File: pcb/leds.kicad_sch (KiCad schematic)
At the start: 0 parts

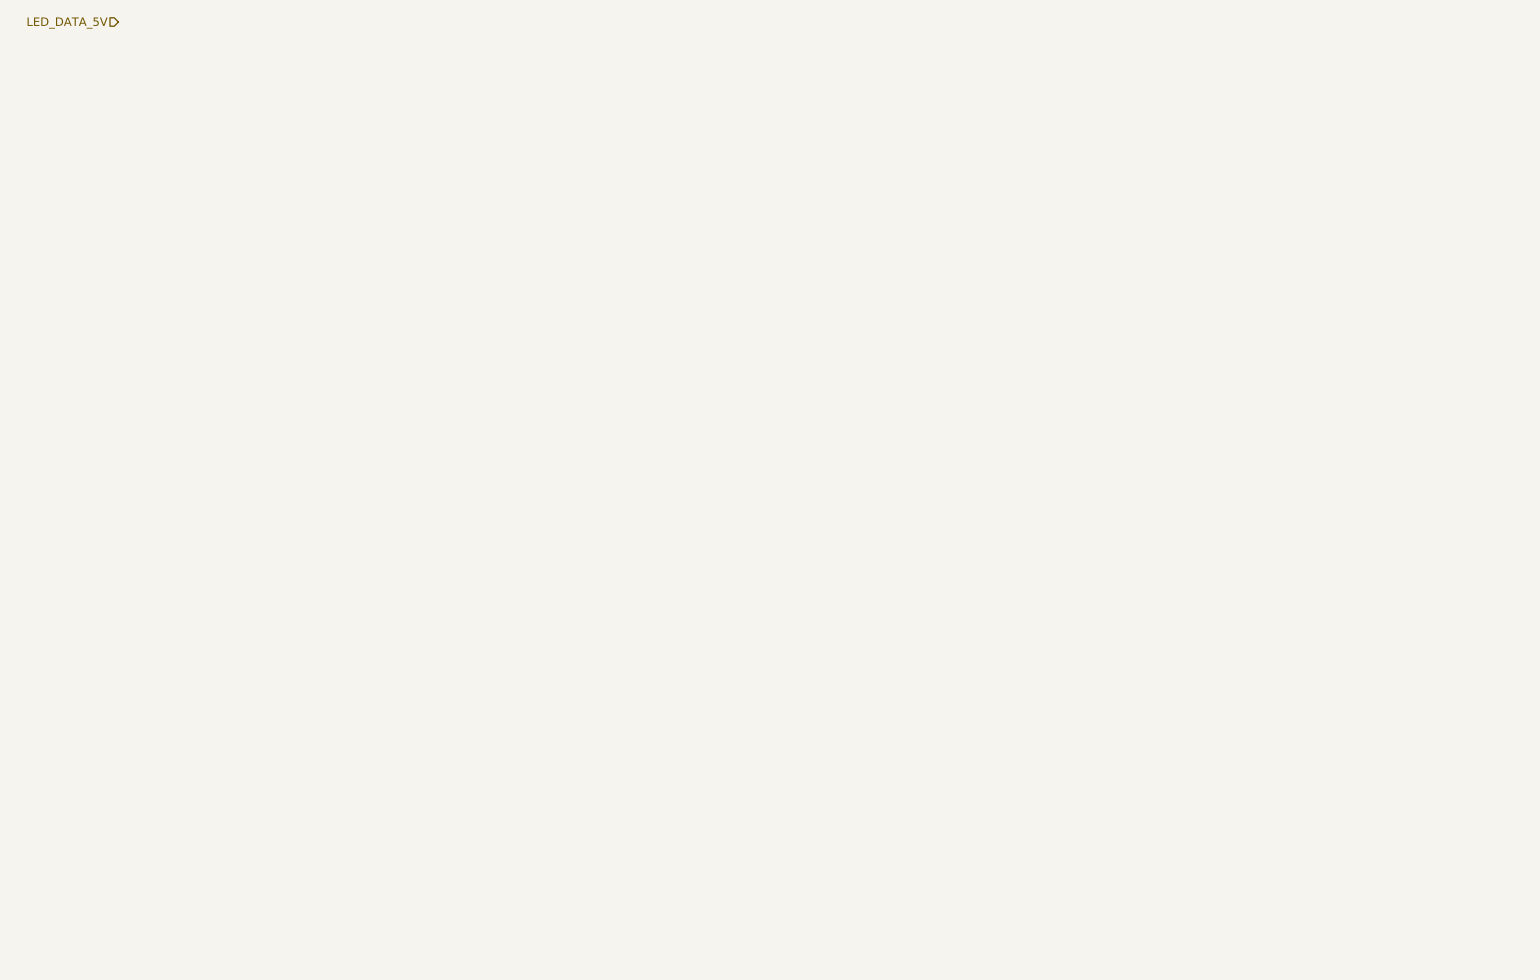
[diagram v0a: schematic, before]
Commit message: Started adding leds and started making pcbs.
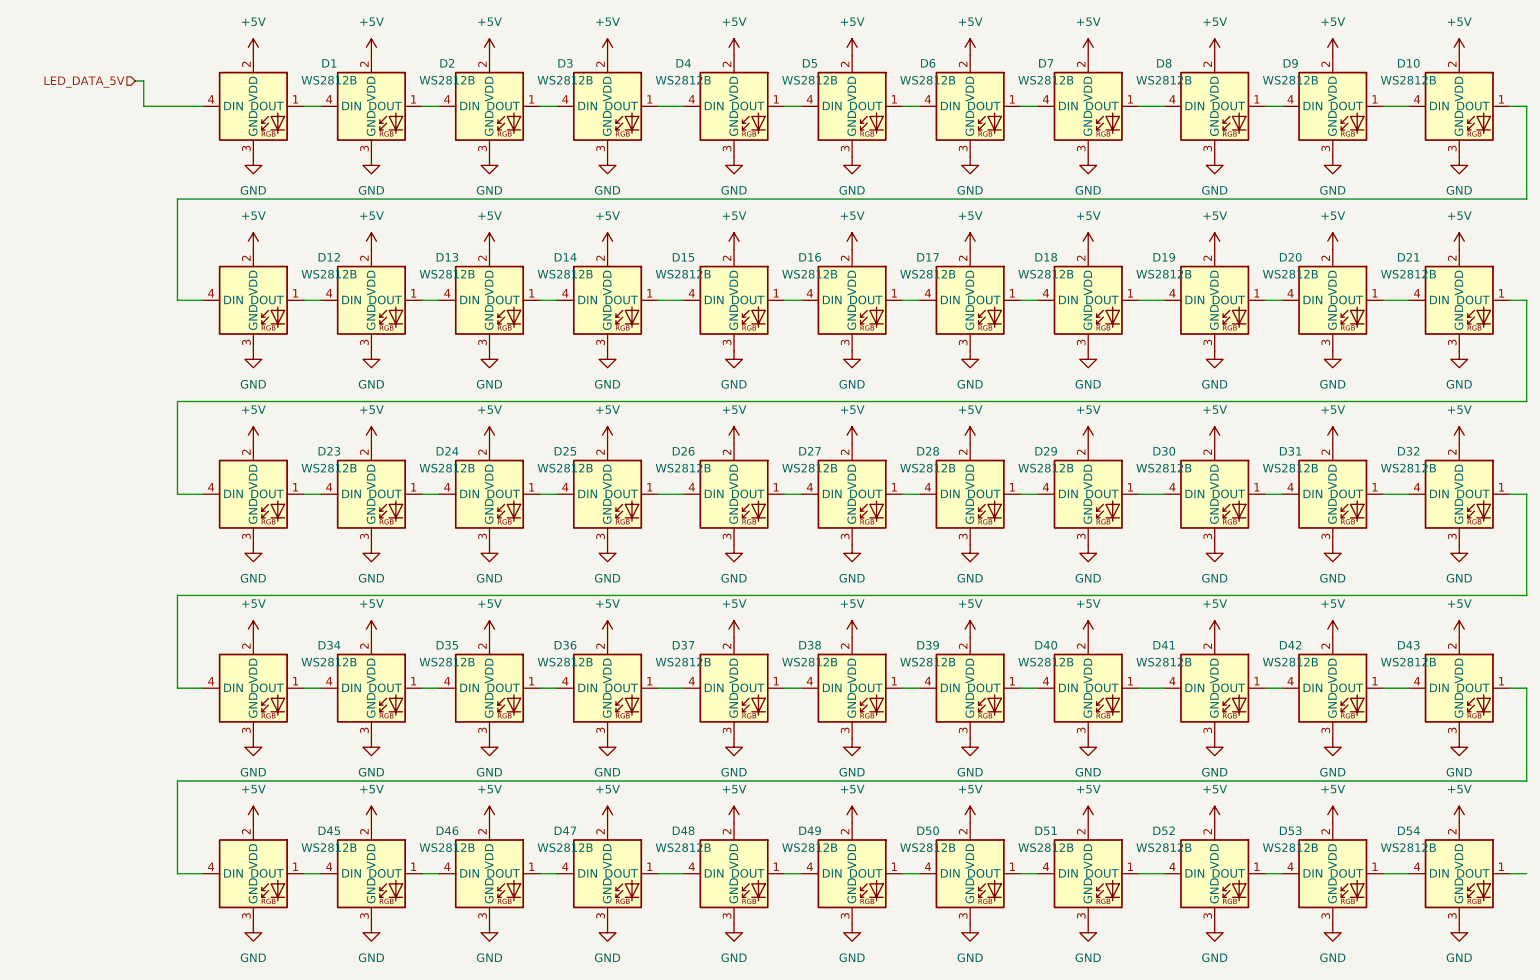
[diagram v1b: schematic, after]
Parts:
- added D1, D10, D11, D12, D13, D14, D15, D16, D17, D18, D19, D2, D20, D21, D22, D23, D24, D25, D26, D27, D28, D29, D3, D30, D31, D32, D33, D34, D35, D36, D37, D38, D39, D4, D40, D41, D42, D43, D44, D45, D46, D47, D48, D49, D5, D50, D51, D52, D53, D54, D55, D6, D7, D8, D9: WS2812B, PCM_JLCPCB:LED-SMD_4P-L1.6-W1.5_XL-1615RGBC-WS2812B, symbol PCM_JLCPCB-Extended:LED, WS2812B, 1615
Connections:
- net LED_DATA_5V: now also D1.4 (DIN)
- new net: D37.1 (DOUT), D38.4 (DIN)
- new net: D36.1 (DOUT), D37.4 (DIN)
- new net: D23.1 (DOUT), D24.4 (DIN)
- new net: D22.1 (DOUT), D23.4 (DIN)
- new net: D10.4 (DIN), D9.1 (DOUT)
- new net: D8.1 (DOUT), D9.4 (DIN)
- new net: D25.1 (DOUT), D26.4 (DIN)
- new net: D24.1 (DOUT), D25.4 (DIN)
- new net: D27.1 (DOUT), D28.4 (DIN)
- new net: D26.1 (DOUT), D27.4 (DIN)
- new net: D1.1 (DOUT), D2.4 (DIN)
- new net: D41.1 (DOUT), D42.4 (DIN)
- new net: D40.1 (DOUT), D41.4 (DIN)
- new net: D5.1 (DOUT), D6.4 (DIN)
- new net: D4.1 (DOUT), D5.4 (DIN)
- new net: D3.1 (DOUT), D4.4 (DIN)
- new net: D46.1 (DOUT), D47.4 (DIN)
- new net: D45.1 (DOUT), D46.4 (DIN)
- new net: D6.1 (DOUT), D7.4 (DIN)
- new net: D43.1 (DOUT), D44.4 (DIN)
- new net: D42.1 (DOUT), D43.4 (DIN)
- new net: D7.1 (DOUT), D8.4 (DIN)
- new net: D13.1 (DOUT), D14.4 (DIN)
- new net: D12.1 (DOUT), D13.4 (DIN)
- new net: D14.1 (DOUT), D15.4 (DIN)
- new net: D17.1 (DOUT), D18.4 (DIN)
- new net: D16.1 (DOUT), D17.4 (DIN)
- new net: D54.1 (DOUT), D55.4 (DIN)
- new net: D53.1 (DOUT), D54.4 (DIN)
- new net: D10.1 (DOUT), D11.4 (DIN)
- new net: D18.1 (DOUT), D19.4 (DIN)
- new net: D20.1 (DOUT), D21.4 (DIN)
- new net: D19.1 (DOUT), D20.4 (DIN)
- new net: D34.1 (DOUT), D35.4 (DIN)
- new net: D33.1 (DOUT), D34.4 (DIN)
- new net: D49.1 (DOUT), D50.4 (DIN)
- new net: D48.1 (DOUT), D49.4 (DIN)
- new net: D11.1 (DOUT), D12.4 (DIN)
- new net: D47.1 (DOUT), D48.4 (DIN)
- new net: D44.1 (DOUT), D45.4 (DIN)
- new net: D39.1 (DOUT), D40.4 (DIN)
- new net: D38.1 (DOUT), D39.4 (DIN)
- new net: D30.1 (DOUT), D31.4 (DIN)
- new net: D29.1 (DOUT), D30.4 (DIN)
- new net: D2.1 (DOUT), D3.4 (DIN)
- new net: D50.1 (DOUT), D51.4 (DIN)
- new net: D52.1 (DOUT), D53.4 (DIN)
- new net: D15.1 (DOUT), D16.4 (DIN)
- new net: D51.1 (DOUT), D52.4 (DIN)
- new net: D31.1 (DOUT), D32.4 (DIN)
- new net: D21.1 (DOUT), D22.4 (DIN)
- new net: D32.1 (DOUT), D33.4 (DIN)
- new net: D35.1 (DOUT), D36.4 (DIN)
- new net: D28.1 (DOUT), D29.4 (DIN)
- new net +5V: D1.2 (VDD), D10.2 (VDD), D11.2 (VDD), D12.2 (VDD), D13.2 (VDD), D14.2 (VDD), D15.2 (VDD), D16.2 (VDD), D17.2 (VDD), D18.2 (VDD), D19.2 (VDD), D2.2 (VDD), D20.2 (VDD), D21.2 (VDD), D22.2 (VDD), D23.2 (VDD), D24.2 (VDD), D25.2 (VDD), D26.2 (VDD), D27.2 (VDD), D28.2 (VDD), D29.2 (VDD), D3.2 (VDD), D30.2 (VDD), D31.2 (VDD), D32.2 (VDD), D33.2 (VDD), D34.2 (VDD), D35.2 (VDD), D36.2 (VDD), D37.2 (VDD), D38.2 (VDD), D39.2 (VDD), D4.2 (VDD), D40.2 (VDD), D41.2 (VDD), D42.2 (VDD), D43.2 (VDD), D44.2 (VDD), D45.2 (VDD), D46.2 (VDD), D47.2 (VDD), D48.2 (VDD), D49.2 (VDD), D5.2 (VDD), D50.2 (VDD), D51.2 (VDD), D52.2 (VDD), D53.2 (VDD), D54.2 (VDD), D55.2 (VDD), D6.2 (VDD), D7.2 (VDD), D8.2 (VDD), D9.2 (VDD)
- new net GND: D1.3 (GND), D10.3 (GND), D11.3 (GND), D12.3 (GND), D13.3 (GND), D14.3 (GND), D15.3 (GND), D16.3 (GND), D17.3 (GND), D18.3 (GND), D19.3 (GND), D2.3 (GND), D20.3 (GND), D21.3 (GND), D22.3 (GND), D23.3 (GND), D24.3 (GND), D25.3 (GND), D26.3 (GND), D27.3 (GND), D28.3 (GND), D29.3 (GND), D3.3 (GND), D30.3 (GND), D31.3 (GND), D32.3 (GND), D33.3 (GND), D34.3 (GND), D35.3 (GND), D36.3 (GND), D37.3 (GND), D38.3 (GND), D39.3 (GND), D4.3 (GND), D40.3 (GND), D41.3 (GND), D42.3 (GND), D43.3 (GND), D44.3 (GND), D45.3 (GND), D46.3 (GND), D47.3 (GND), D48.3 (GND), D49.3 (GND), D5.3 (GND), D50.3 (GND), D51.3 (GND), D52.3 (GND), D53.3 (GND), D54.3 (GND), D55.3 (GND), D6.3 (GND), D7.3 (GND), D8.3 (GND), D9.3 (GND)

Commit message: server updates and battling with kicad
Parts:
- removed D10, D11, D12, D13, D14, D15, D16, D17, D18, D19, D2, D20, D21, D22, D23, D24, D25, D26, D27, D28, D29, D3, D30, D31, D32, D33, D34, D35, D36, D37, D38, D39, D4, D40, D41, D42, D43, D44, D45, D46, D47, D48, D49, D5, D50, D51, D52, D53, D54, D55, D6, D7, D8, D9: WS2812B, PCM_JLCPCB:LED-SMD_4P-L1.6-W1.5_XL-1615RGBC-WS2812B, symbol PCM_JLCPCB-Extended:LED, WS2812B, 1615
- added D102, D103, D104, D105, D106, D107, D108, D109, D110, D111, D112, D113, D114, D115, D116, D117, D118, D119, D120, D121, D122, D123, D124, D125, D126, D127, D128, D129, D130, D131, D132, D133, D134, D135, D136, D137, D138, D139, D140, D141, D142, D143, D144, D145, D146, D147, D148, D149, D150, D151, D152, D153, D154, D155, D156, D157, D158, D159, D160, D161, D162, D163, D164, D165, D166, D167, D168, D169, D170, D171, D172, D173, D174, D175, D176, D177, D178, D179, D180, D181, D182, D183, D184, D185, D186, D187, D188, D189, D190, D191, D192, D193, D194, D195, D196, D197, D198, D199, D200: WS2812B, PCM_JLCPCB:LED-SMD_4P-L1.6-W1.5_XL-1615RGBC-WS2812B, symbol PCM_JLCPCB-Extended:LED, WS2812B, 1615
- renumbered D1 to D101
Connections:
- net +5V: now also D102.2 (VDD), D103.2 (VDD), D104.2 (VDD), D105.2 (VDD), D106.2 (VDD), D107.2 (VDD), D108.2 (VDD), D109.2 (VDD), D110.2 (VDD), D111.2 (VDD), D112.2 (VDD), D113.2 (VDD), D114.2 (VDD), D115.2 (VDD), D116.2 (VDD), D117.2 (VDD), D118.2 (VDD), D119.2 (VDD), D120.2 (VDD), D121.2 (VDD), D122.2 (VDD), D123.2 (VDD), D124.2 (VDD), D125.2 (VDD), D126.2 (VDD), D127.2 (VDD), D128.2 (VDD), D129.2 (VDD), D130.2 (VDD), D131.2 (VDD), D132.2 (VDD), D133.2 (VDD), D134.2 (VDD), D135.2 (VDD), D136.2 (VDD), D137.2 (VDD), D138.2 (VDD), D139.2 (VDD), D140.2 (VDD), D141.2 (VDD), D142.2 (VDD), D143.2 (VDD), D144.2 (VDD), D145.2 (VDD), D146.2 (VDD), D147.2 (VDD), D148.2 (VDD), D149.2 (VDD), D150.2 (VDD), D151.2 (VDD), D152.2 (VDD), D153.2 (VDD), D154.2 (VDD), D155.2 (VDD), D156.2 (VDD), D157.2 (VDD), D158.2 (VDD), D159.2 (VDD), D160.2 (VDD), D161.2 (VDD), D162.2 (VDD), D163.2 (VDD), D164.2 (VDD), D165.2 (VDD), D166.2 (VDD), D167.2 (VDD), D168.2 (VDD), D169.2 (VDD), D170.2 (VDD), D171.2 (VDD), D172.2 (VDD), D173.2 (VDD), D174.2 (VDD), D175.2 (VDD), D176.2 (VDD), D177.2 (VDD), D178.2 (VDD), D179.2 (VDD), D180.2 (VDD), D181.2 (VDD), D182.2 (VDD), D183.2 (VDD), D184.2 (VDD), D185.2 (VDD), D186.2 (VDD), D187.2 (VDD), D188.2 (VDD), D189.2 (VDD), D190.2 (VDD), D191.2 (VDD), D192.2 (VDD), D193.2 (VDD), D194.2 (VDD), D195.2 (VDD), D196.2 (VDD), D197.2 (VDD), D198.2 (VDD), D199.2 (VDD), D200.2 (VDD)
- net GND: now also D102.3 (GND), D103.3 (GND), D104.3 (GND), D105.3 (GND), D106.3 (GND), D107.3 (GND), D108.3 (GND), D109.3 (GND), D110.3 (GND), D111.3 (GND), D112.3 (GND), D113.3 (GND), D114.3 (GND), D115.3 (GND), D116.3 (GND), D117.3 (GND), D118.3 (GND), D119.3 (GND), D120.3 (GND), D121.3 (GND), D122.3 (GND), D123.3 (GND), D124.3 (GND), D125.3 (GND), D126.3 (GND), D127.3 (GND), D128.3 (GND), D129.3 (GND), D130.3 (GND), D131.3 (GND), D132.3 (GND), D133.3 (GND), D134.3 (GND), D135.3 (GND), D136.3 (GND), D137.3 (GND), D138.3 (GND), D139.3 (GND), D140.3 (GND), D141.3 (GND), D142.3 (GND), D143.3 (GND), D144.3 (GND), D145.3 (GND), D146.3 (GND), D147.3 (GND), D148.3 (GND), D149.3 (GND), D150.3 (GND), D151.3 (GND), D152.3 (GND), D153.3 (GND), D154.3 (GND), D155.3 (GND), D156.3 (GND), D157.3 (GND), D158.3 (GND), D159.3 (GND), D160.3 (GND), D161.3 (GND), D162.3 (GND), D163.3 (GND), D164.3 (GND), D165.3 (GND), D166.3 (GND), D167.3 (GND), D168.3 (GND), D169.3 (GND), D170.3 (GND), D171.3 (GND), D172.3 (GND), D173.3 (GND), D174.3 (GND), D175.3 (GND), D176.3 (GND), D177.3 (GND), D178.3 (GND), D179.3 (GND), D180.3 (GND), D181.3 (GND), D182.3 (GND), D183.3 (GND), D184.3 (GND), D185.3 (GND), D186.3 (GND), D187.3 (GND), D188.3 (GND), D189.3 (GND), D190.3 (GND), D191.3 (GND), D192.3 (GND), D193.3 (GND), D194.3 (GND), D195.3 (GND), D196.3 (GND), D197.3 (GND), D198.3 (GND), D199.3 (GND), D200.3 (GND)
- net at D101.1 (DOUT): now also D102.4 (DIN)
- new net: D134.1 (DOUT), D135.4 (DIN)
- new net: D133.1 (DOUT), D134.4 (DIN)
- new net: D187.1 (DOUT), D188.4 (DIN)
- new net: D186.1 (DOUT), D187.4 (DIN)
- new net: D160.1 (DOUT), D161.4 (DIN)
- new net: D159.1 (DOUT), D160.4 (DIN)
- new net: D149.1 (DOUT), D150.4 (DIN)
- new net: D148.1 (DOUT), D149.4 (DIN)
- new net: D180.1 (DOUT), D181.4 (DIN)
- new net: D179.1 (DOUT), D180.4 (DIN)
- new net: D116.1 (DOUT), D117.4 (DIN)
- new net: D115.1 (DOUT), D116.4 (DIN)
- new net: D195.1 (DOUT), D196.4 (DIN)
- new net: D194.1 (DOUT), D195.4 (DIN)
- new net: D141.1 (DOUT), D142.4 (DIN)
- new net: D140.1 (DOUT), D141.4 (DIN)
- new net: D163.1 (DOUT), D164.4 (DIN)
- new net: D162.1 (DOUT), D163.4 (DIN)
- new net: D193.1 (DOUT), D194.4 (DIN)
- new net: D192.1 (DOUT), D193.4 (DIN)
- new net: D183.1 (DOUT), D184.4 (DIN)
- new net: D182.1 (DOUT), D183.4 (DIN)
- new net: D161.1 (DOUT), D162.4 (DIN)
- new net: D171.1 (DOUT), D172.4 (DIN)
- new net: D170.1 (DOUT), D171.4 (DIN)
- new net: D185.1 (DOUT), D186.4 (DIN)
- new net: D132.1 (DOUT), D133.4 (DIN)
- new net: D165.1 (DOUT), D166.4 (DIN)
- new net: D164.1 (DOUT), D165.4 (DIN)
- new net: D156.1 (DOUT), D157.4 (DIN)
- new net: D155.1 (DOUT), D156.4 (DIN)
- new net: D181.1 (DOUT), D182.4 (DIN)
- new net: D113.1 (DOUT), D114.4 (DIN)
- new net: D112.1 (DOUT), D113.4 (DIN)
- new net: D138.1 (DOUT), D139.4 (DIN)
- new net: D137.1 (DOUT), D138.4 (DIN)
- new net: D168.1 (DOUT), D169.4 (DIN)
- new net: D167.1 (DOUT), D168.4 (DIN)
- new net: D197.1 (DOUT), D198.4 (DIN)
- new net: D196.1 (DOUT), D197.4 (DIN)
- new net: D188.1 (DOUT), D189.4 (DIN)
- new net: D199.1 (DOUT), D200.4 (DIN)
- new net: D126.1 (DOUT), D127.4 (DIN)
- new net: D125.1 (DOUT), D126.4 (DIN)
- new net: D106.1 (DOUT), D107.4 (DIN)
- new net: D105.1 (DOUT), D106.4 (DIN)
- new net: D108.1 (DOUT), D109.4 (DIN)
- new net: D107.1 (DOUT), D108.4 (DIN)
- new net: D169.1 (DOUT), D170.4 (DIN)
- new net: D109.1 (DOUT), D110.4 (DIN)
- new net: D103.1 (DOUT), D104.4 (DIN)
- new net: D102.1 (DOUT), D103.4 (DIN)
- new net: D198.1 (DOUT), D199.4 (DIN)
- new net: D111.1 (DOUT), D112.4 (DIN)
- new net: D110.1 (DOUT), D111.4 (DIN)
- new net: D118.1 (DOUT), D119.4 (DIN)
- new net: D117.1 (DOUT), D118.4 (DIN)
- new net: D130.1 (DOUT), D131.4 (DIN)
- new net: D129.1 (DOUT), D130.4 (DIN)
- new net: D178.1 (DOUT), D179.4 (DIN)
- new net: D114.1 (DOUT), D115.4 (DIN)
- new net: D158.1 (DOUT), D159.4 (DIN)
- new net: D157.1 (DOUT), D158.4 (DIN)
- new net: D144.1 (DOUT), D145.4 (DIN)
- new net: D143.1 (DOUT), D144.4 (DIN)
- new net: D189.1 (DOUT), D190.4 (DIN)
- new net: D147.1 (DOUT), D148.4 (DIN)
- new net: D146.1 (DOUT), D147.4 (DIN)
- new net: D151.1 (DOUT), D152.4 (DIN)
- new net: D150.1 (DOUT), D151.4 (DIN)
- new net: D190.1 (DOUT), D191.4 (DIN)
- new net: D119.1 (DOUT), D120.4 (DIN)
- new net: D124.1 (DOUT), D125.4 (DIN)
- new net: D122.1 (DOUT), D123.4 (DIN)
- new net: D121.1 (DOUT), D122.4 (DIN)
- new net: D174.1 (DOUT), D175.4 (DIN)
- new net: D173.1 (DOUT), D174.4 (DIN)
- new net: D184.1 (DOUT), D185.4 (DIN)
- new net: D172.1 (DOUT), D173.4 (DIN)
- new net: D142.1 (DOUT), D143.4 (DIN)
- new net: D123.1 (DOUT), D124.4 (DIN)
- new net: D128.1 (DOUT), D129.4 (DIN)
- new net: D175.1 (DOUT), D176.4 (DIN)
- new net: D120.1 (DOUT), D121.4 (DIN)
- new net: D154.1 (DOUT), D155.4 (DIN)
- new net: D153.1 (DOUT), D154.4 (DIN)
- new net: D145.1 (DOUT), D146.4 (DIN)
- new net: D166.1 (DOUT), D167.4 (DIN)
- new net: D135.1 (DOUT), D136.4 (DIN)
- new net: D152.1 (DOUT), D153.4 (DIN)
- new net: D131.1 (DOUT), D132.4 (DIN)
- new net: D104.1 (DOUT), D105.4 (DIN)
- new net: D177.1 (DOUT), D178.4 (DIN)
- new net: D139.1 (DOUT), D140.4 (DIN)
- new net: D191.1 (DOUT), D192.4 (DIN)
- new net: D136.1 (DOUT), D137.4 (DIN)
- new net: D176.1 (DOUT), D177.4 (DIN)
- new net: D127.1 (DOUT), D128.4 (DIN)
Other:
- moved on the sheet: D101

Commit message: finished pcb routing
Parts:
- added D201, D202, D203, D204, D205, D206, D207, D208, D209, D210, D211, D212, D213, D214, D215, D216, D217, D218, D219, D220, D221, D222, D223, D224, D225, D226, D227, D228, D229, D230, D231, D232, D233, D234, D235, D236, D237, D238, D239, D240, D241, D242, D243, D244, D245, D246, D247, D248, D249, D250, D251, D252, D253, D254, D255, D256, D257, D258, D259, D260, D261, D262, D263, D264, D265, D266, D267, D268, D269, D270, D271, D272, D273, D274, D275, D276, D277, D278, D279, D280, D281, D282, D283, D284, D285, D286, D287, D288, D289, D290, D291, D292, D293, D294, D295, D296, D297, D298, D299, D300, D301, D302, D303, D304, D305, D306, D307, D308, D309, D310, D311, D312, D313, D314, D315, D316, D317, D318, D319, D320, D321, D322, D323, D324, D325, D326, D327, D328, D329, D330, D331, D332, D333, D334, D335, D336, D337, D338, D339: WS2812B, PCM_JLCPCB:LED-SMD_4P-L1.6-W1.5_XL-1615RGBC-WS2812B, symbol PCM_JLCPCB-Extended:LED, WS2812B, 1615
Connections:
- net +5V: now also D201.2 (VDD), D202.2 (VDD), D203.2 (VDD), D204.2 (VDD), D205.2 (VDD), D206.2 (VDD), D207.2 (VDD), D208.2 (VDD), D209.2 (VDD), D210.2 (VDD), D211.2 (VDD), D212.2 (VDD), D213.2 (VDD), D214.2 (VDD), D215.2 (VDD), D216.2 (VDD), D217.2 (VDD), D218.2 (VDD), D219.2 (VDD), D220.2 (VDD), D221.2 (VDD), D222.2 (VDD), D223.2 (VDD), D224.2 (VDD), D225.2 (VDD), D226.2 (VDD), D227.2 (VDD), D228.2 (VDD), D229.2 (VDD), D230.2 (VDD), D231.2 (VDD), D232.2 (VDD), D233.2 (VDD), D234.2 (VDD), D235.2 (VDD), D236.2 (VDD), D237.2 (VDD), D238.2 (VDD), D239.2 (VDD), D240.2 (VDD), D241.2 (VDD), D242.2 (VDD), D243.2 (VDD), D244.2 (VDD), D245.2 (VDD), D246.2 (VDD), D247.2 (VDD), D248.2 (VDD), D249.2 (VDD), D250.2 (VDD), D251.2 (VDD), D252.2 (VDD), D253.2 (VDD), D254.2 (VDD), D255.2 (VDD), D256.2 (VDD), D257.2 (VDD), D258.2 (VDD), D259.2 (VDD), D260.2 (VDD), D261.2 (VDD), D262.2 (VDD), D263.2 (VDD), D264.2 (VDD), D265.2 (VDD), D266.2 (VDD), D267.2 (VDD), D268.2 (VDD), D269.2 (VDD), D270.2 (VDD), D271.2 (VDD), D272.2 (VDD), D273.2 (VDD), D274.2 (VDD), D275.2 (VDD), D276.2 (VDD), D277.2 (VDD), D278.2 (VDD), D279.2 (VDD), D280.2 (VDD), D281.2 (VDD), D282.2 (VDD), D283.2 (VDD), D284.2 (VDD), D285.2 (VDD), D286.2 (VDD), D287.2 (VDD), D288.2 (VDD), D289.2 (VDD), D290.2 (VDD), D291.2 (VDD), D292.2 (VDD), D293.2 (VDD), D294.2 (VDD), D295.2 (VDD), D296.2 (VDD), D297.2 (VDD), D298.2 (VDD), D299.2 (VDD), D300.2 (VDD), D301.2 (VDD), D302.2 (VDD), D303.2 (VDD), D304.2 (VDD), D305.2 (VDD), D306.2 (VDD), D307.2 (VDD), D308.2 (VDD), D309.2 (VDD), D310.2 (VDD), D311.2 (VDD), D312.2 (VDD), D313.2 (VDD), D314.2 (VDD), D315.2 (VDD), D316.2 (VDD), D317.2 (VDD), D318.2 (VDD), D319.2 (VDD), D320.2 (VDD), D321.2 (VDD), D322.2 (VDD), D323.2 (VDD), D324.2 (VDD), D325.2 (VDD), D326.2 (VDD), D327.2 (VDD), D328.2 (VDD), D329.2 (VDD), D330.2 (VDD), D331.2 (VDD), D332.2 (VDD), D333.2 (VDD), D334.2 (VDD), D335.2 (VDD), D336.2 (VDD), D337.2 (VDD), D338.2 (VDD), D339.2 (VDD)
- net GND: now also D201.3 (GND), D202.3 (GND), D203.3 (GND), D204.3 (GND), D205.3 (GND), D206.3 (GND), D207.3 (GND), D208.3 (GND), D209.3 (GND), D210.3 (GND), D211.3 (GND), D212.3 (GND), D213.3 (GND), D214.3 (GND), D215.3 (GND), D216.3 (GND), D217.3 (GND), D218.3 (GND), D219.3 (GND), D220.3 (GND), D221.3 (GND), D222.3 (GND), D223.3 (GND), D224.3 (GND), D225.3 (GND), D226.3 (GND), D227.3 (GND), D228.3 (GND), D229.3 (GND), D230.3 (GND), D231.3 (GND), D232.3 (GND), D233.3 (GND), D234.3 (GND), D235.3 (GND), D236.3 (GND), D237.3 (GND), D238.3 (GND), D239.3 (GND), D240.3 (GND), D241.3 (GND), D242.3 (GND), D243.3 (GND), D244.3 (GND), D245.3 (GND), D246.3 (GND), D247.3 (GND), D248.3 (GND), D249.3 (GND), D250.3 (GND), D251.3 (GND), D252.3 (GND), D253.3 (GND), D254.3 (GND), D255.3 (GND), D256.3 (GND), D257.3 (GND), D258.3 (GND), D259.3 (GND), D260.3 (GND), D261.3 (GND), D262.3 (GND), D263.3 (GND), D264.3 (GND), D265.3 (GND), D266.3 (GND), D267.3 (GND), D268.3 (GND), D269.3 (GND), D270.3 (GND), D271.3 (GND), D272.3 (GND), D273.3 (GND), D274.3 (GND), D275.3 (GND), D276.3 (GND), D277.3 (GND), D278.3 (GND), D279.3 (GND), D280.3 (GND), D281.3 (GND), D282.3 (GND), D283.3 (GND), D284.3 (GND), D285.3 (GND), D286.3 (GND), D287.3 (GND), D288.3 (GND), D289.3 (GND), D290.3 (GND), D291.3 (GND), D292.3 (GND), D293.3 (GND), D294.3 (GND), D295.3 (GND), D296.3 (GND), D297.3 (GND), D298.3 (GND), D299.3 (GND), D300.3 (GND), D301.3 (GND), D302.3 (GND), D303.3 (GND), D304.3 (GND), D305.3 (GND), D306.3 (GND), D307.3 (GND), D308.3 (GND), D309.3 (GND), D310.3 (GND), D311.3 (GND), D312.3 (GND), D313.3 (GND), D314.3 (GND), D315.3 (GND), D316.3 (GND), D317.3 (GND), D318.3 (GND), D319.3 (GND), D320.3 (GND), D321.3 (GND), D322.3 (GND), D323.3 (GND), D324.3 (GND), D325.3 (GND), D326.3 (GND), D327.3 (GND), D328.3 (GND), D329.3 (GND), D330.3 (GND), D331.3 (GND), D332.3 (GND), D333.3 (GND), D334.3 (GND), D335.3 (GND), D336.3 (GND), D337.3 (GND), D338.3 (GND), D339.3 (GND)
- net at D200.1 (DOUT): now also D201.4 (DIN)
- new net: D260.1 (DOUT), D261.4 (DIN)
- new net: D259.1 (DOUT), D260.4 (DIN)
- new net: D263.1 (DOUT), D264.4 (DIN)
- new net: D262.1 (DOUT), D263.4 (DIN)
- new net: D273.1 (DOUT), D274.4 (DIN)
- new net: D272.1 (DOUT), D273.4 (DIN)
- new net: D324.1 (DOUT), D325.4 (DIN)
- new net: D323.1 (DOUT), D324.4 (DIN)
- new net: D249.1 (DOUT), D250.4 (DIN)
- new net: D248.1 (DOUT), D249.4 (DIN)
- new net: D294.1 (DOUT), D295.4 (DIN)
- new net: D293.1 (DOUT), D294.4 (DIN)
- new net: D254.1 (DOUT), D255.4 (DIN)
- new net: D253.1 (DOUT), D254.4 (DIN)
- new net: D309.1 (DOUT), D310.4 (DIN)
- new net: D308.1 (DOUT), D309.4 (DIN)
- new net: D306.1 (DOUT), D307.4 (DIN)
- new net: D305.1 (DOUT), D306.4 (DIN)
- new net: D276.1 (DOUT), D277.4 (DIN)
- new net: D275.1 (DOUT), D276.4 (DIN)
- new net: D215.1 (DOUT), D216.4 (DIN)
- new net: D214.1 (DOUT), D215.4 (DIN)
- new net: D203.1 (DOUT), D204.4 (DIN)
- new net: D202.1 (DOUT), D203.4 (DIN)
- new net: D222.1 (DOUT), D223.4 (DIN)
- new net: D221.1 (DOUT), D222.4 (DIN)
- new net: D301.1 (DOUT), D302.4 (DIN)
- new net: D300.1 (DOUT), D301.4 (DIN)
- new net: D261.1 (DOUT), D262.4 (DIN)
- new net: D244.1 (DOUT), D245.4 (DIN)
- new net: D243.1 (DOUT), D244.4 (DIN)
- new net: D271.1 (DOUT), D272.4 (DIN)
- new net: D311.1 (DOUT), D312.4 (DIN)
- new net: D310.1 (DOUT), D311.4 (DIN)
- new net: D329.1 (DOUT), D330.4 (DIN)
- new net: D328.1 (DOUT), D329.4 (DIN)
- new net: D334.1 (DOUT), D335.4 (DIN)
- new net: D333.1 (DOUT), D334.4 (DIN)
- new net: D298.1 (DOUT), D299.4 (DIN)
- new net: D297.1 (DOUT), D298.4 (DIN)
- new net: D282.1 (DOUT), D283.4 (DIN)
- new net: D281.1 (DOUT), D282.4 (DIN)
- new net: D235.1 (DOUT), D236.4 (DIN)
- new net: D234.1 (DOUT), D235.4 (DIN)
- new net: D291.1 (DOUT), D292.4 (DIN)
- new net: D290.1 (DOUT), D291.4 (DIN)
- new net: D278.1 (DOUT), D279.4 (DIN)
- new net: D277.1 (DOUT), D278.4 (DIN)
- new net: D307.1 (DOUT), D308.4 (DIN)
- new net: D229.1 (DOUT), D230.4 (DIN)
- new net: D228.1 (DOUT), D229.4 (DIN)
- new net: D220.1 (DOUT), D221.4 (DIN)
- new net: D219.1 (DOUT), D220.4 (DIN)
- new net: D218.1 (DOUT), D219.4 (DIN)
- new net: D268.1 (DOUT), D269.4 (DIN)
- new net: D267.1 (DOUT), D268.4 (DIN)
- new net: D283.1 (DOUT), D284.4 (DIN)
- new net: D241.1 (DOUT), D242.4 (DIN)
- new net: D240.1 (DOUT), D241.4 (DIN)
- new net: D201.1 (DOUT), D202.4 (DIN)
- new net: D318.1 (DOUT), D319.4 (DIN)
- new net: D317.1 (DOUT), D318.4 (DIN)
- new net: D233.1 (DOUT), D234.4 (DIN)
- new net: D270.1 (DOUT), D271.4 (DIN)
- new net: D269.1 (DOUT), D270.4 (DIN)
- new net: D208.1 (DOUT), D209.4 (DIN)
- new net: D207.1 (DOUT), D208.4 (DIN)
- new net: D206.1 (DOUT), D207.4 (DIN)
- new net: D205.1 (DOUT), D206.4 (DIN)
- new net: D223.1 (DOUT), D224.4 (DIN)
- new net: D204.1 (DOUT), D205.4 (DIN)
- new net: D225.1 (DOUT), D226.4 (DIN)
- new net: D224.1 (DOUT), D225.4 (DIN)
- new net: D258.1 (DOUT), D259.4 (DIN)
- new net: D315.1 (DOUT), D316.4 (DIN)
- new net: D314.1 (DOUT), D315.4 (DIN)
- new net: D304.1 (DOUT), D305.4 (DIN)
- new net: D338.1 (DOUT), D339.4 (DIN)
- new net: D337.1 (DOUT), D338.4 (DIN)
- new net: D299.1 (DOUT), D300.4 (DIN)
- new net: D313.1 (DOUT), D314.4 (DIN)
- new net: D316.1 (DOUT), D317.4 (DIN)
- new net: D230.1 (DOUT), D231.4 (DIN)
- new net: D285.1 (DOUT), D286.4 (DIN)
- new net: D284.1 (DOUT), D285.4 (DIN)
- new net: D280.1 (DOUT), D281.4 (DIN)
- new net: D279.1 (DOUT), D280.4 (DIN)
- new net: D335.1 (DOUT), D336.4 (DIN)
- new net: D231.1 (DOUT), D232.4 (DIN)
- new net: D250.1 (DOUT), D251.4 (DIN)
- new net: D286.1 (DOUT), D287.4 (DIN)
- new net: D303.1 (DOUT), D304.4 (DIN)
- new net: D255.1 (DOUT), D256.4 (DIN)
- new net: D289.1 (DOUT), D290.4 (DIN)
- new net: D288.1 (DOUT), D289.4 (DIN)
- new net: D237.1 (DOUT), D238.4 (DIN)
- new net: D236.1 (DOUT), D237.4 (DIN)
- new net: D330.1 (DOUT), D331.4 (DIN)
- new net: D217.1 (DOUT), D218.4 (DIN)
- new net: D252.1 (DOUT), D253.4 (DIN)
- new net: D327.1 (DOUT), D328.4 (DIN)
- new net: D326.1 (DOUT), D327.4 (DIN)
- new net: D266.1 (DOUT), D267.4 (DIN)
- new net: D265.1 (DOUT), D266.4 (DIN)
- new net: D257.1 (DOUT), D258.4 (DIN)
- new net: D264.1 (DOUT), D265.4 (DIN)
- new net: D238.1 (DOUT), D239.4 (DIN)
- new net: D336.1 (DOUT), D337.4 (DIN)
- new net: D332.1 (DOUT), D333.4 (DIN)
- new net: D331.1 (DOUT), D332.4 (DIN)
- new net: D216.1 (DOUT), D217.4 (DIN)
- new net: D251.1 (DOUT), D252.4 (DIN)
- new net: D213.1 (DOUT), D214.4 (DIN)
- new net: D211.1 (DOUT), D212.4 (DIN)
- new net: D210.1 (DOUT), D211.4 (DIN)
- new net: D296.1 (DOUT), D297.4 (DIN)
- new net: D245.1 (DOUT), D246.4 (DIN)
- new net: D209.1 (DOUT), D210.4 (DIN)
- new net: D242.1 (DOUT), D243.4 (DIN)
- new net: D292.1 (DOUT), D293.4 (DIN)
- new net: D232.1 (DOUT), D233.4 (DIN)
- new net: D319.1 (DOUT), D320.4 (DIN)
- new net: D274.1 (DOUT), D275.4 (DIN)
- new net: D246.1 (DOUT), D247.4 (DIN)
- new net: D322.1 (DOUT), D323.4 (DIN)
- new net: D302.1 (DOUT), D303.4 (DIN)
- new net: D212.1 (DOUT), D213.4 (DIN)
- new net: D239.1 (DOUT), D240.4 (DIN)
- new net: D227.1 (DOUT), D228.4 (DIN)
- new net: D226.1 (DOUT), D227.4 (DIN)
- new net: D247.1 (DOUT), D248.4 (DIN)
- new net: D321.1 (DOUT), D322.4 (DIN)
- new net: D320.1 (DOUT), D321.4 (DIN)
- new net: D325.1 (DOUT), D326.4 (DIN)
- new net: D295.1 (DOUT), D296.4 (DIN)
- new net: D287.1 (DOUT), D288.4 (DIN)
- new net: D256.1 (DOUT), D257.4 (DIN)
- new net: D312.1 (DOUT), D313.4 (DIN)
- no-connect marks 0 -> 1
